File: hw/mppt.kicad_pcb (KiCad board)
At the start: 2 copper layers, 7 parts, among them J1 Conn_01x02, J2 Conn_01x02, Q1 Q_NMOS_DGS, Q2 Q_NMOS_DGS

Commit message: working on documentation, design methmethodology, sizing, layout
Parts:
- removed C1: 10uF, Capacitor_SMD:C_1210_3225Metric
- removed C2: 330uF, Capacitor_THT:CP_Radial_D18.0mm_P7.50mm
- removed J1, J2: Conn_01x02, Connector_PinHeader_2.54mm:PinHeader_1x02_P2.54mm_Horizontal
- removed L1: 1529uH, Inductor_THT:L_CommonMode_Toroid_Vertical_L43.2mm_W22.9mm_Px17.78mm_Py30.48mm_Bourns_8100
- removed Q1, Q2: Q_NMOS_DGS, Package_TO_SOT_SMD:TO-263-2
- added C201: 100nF, Capacitor_SMD:C_0402_1005Metric, B.Cu at (183.2, 77.6)
- added C301: 5uF, Capacitor_THT:CP_Axial_L10.0mm_D6.0mm_P15.00mm_Horizontal, F.Cu at (116.5, 108.8)
- added C302: 18uF, Capacitor_THT:CP_Radial_D10.0mm_P5.00mm, F.Cu at (165.0, 109.6)
- added C303: 18uF, Capacitor_THT:CP_Radial_D10.0mm_P5.00mm, F.Cu at (152.5, 109.5)
- added C304: 18uF, Capacitor_THT:CP_Radial_D10.0mm_P5.00mm, F.Cu at (162.3, 95.5)
- added C401: 100nF, Capacitor_SMD:C_0805_2012Metric, B.Cu at (114.2, 85.4)
- added C402: 100nF, Capacitor_SMD:C_0805_2012Metric, B.Cu at (177.7, 85.6)
- added C403: 100nF, Capacitor_SMD:C_0805_2012Metric, B.Cu at (114.2, 81.4)
- added C404: 100nF, Capacitor_SMD:C_0805_2012Metric, B.Cu at (169.0, 82.6)
- added D202: BLUE, LED_SMD:LED_0805_2012Metric, F.Cu at (107.7, 61.9)
- added D203: YELLOW, LED_SMD:LED_0805_2012Metric, F.Cu at (107.7, 65.0)
- added D204: RED, LED_SMD:LED_0805_2012Metric, F.Cu at (107.7, 68.0)
- added D401: 3.3V Zener, Diode_SMD:D_MiniMELF, B.Cu at (109.5, 82.3)
- added D402: 3.3V Zener, Diode_SMD:D_MiniMELF, B.Cu at (173.6, 82.4)
- added D403: 3.3V Zener, Diode_SMD:D_MiniMELF, B.Cu at (121.7, 81.5)
- added D404: 3.3V Zener, Diode_SMD:D_MiniMELF, B.Cu at (161.5, 81.7)
- added H101: Top Left Mounting Hole, MountingHole:MountingHole_2.2mm_M2, F.Cu at (95.1, 64.9)
- added H102: Top Right Mounting Hole, MountingHole:MountingHole_2.2mm_M2, F.Cu at (187.5, 62.8)
- added H103: Bottom Left Mounting Hole, MountingHole:MountingHole_2.2mm_M2, F.Cu at (94.5, 110.3)
- added H104: Bottom Right Mounting Hole, MountingHole:MountingHole_2.2mm_M2, F.Cu at (188.8, 110.3)
- added J201: 1935776, mppt:1935776, F.Cu at (186.4, 75.1)
- added J301: 1935776, mppt:1935776, F.Cu at (100.2, 103.8)
- added J302: 1935776, mppt:1935776, F.Cu at (183.2, 103.8)
- added Q301: Q_NMOS_DGS, mppt:EPC2307, F.Cu at (152.5, 97.8)
- added Q302: Q_NMOS_DGS, mppt:EPC2307, F.Cu at (156.9, 97.8)
- added R201: 330, Resistor_SMD:R_0805_2012Metric, F.Cu at (112.1, 61.9)
- added R202: 330, Resistor_SMD:R_0805_2012Metric, F.Cu at (112.1, 64.9)
- added R203: 330, Resistor_SMD:R_0805_2012Metric, F.Cu at (112.1, 67.8)
- added R401: 2m, Resistor_SMD:R_1206_3216Metric, F.Cu at (110.0, 98.8)
- added R402: 2m, Resistor_SMD:R_1206_3216Metric, F.Cu at (173.4, 95.5)
- added R403: 100k, Resistor_SMD:R_0805_2012Metric, B.Cu at (118.1, 86.1)
- added R404: 3k, Resistor_SMD:R_0805_2012Metric, B.Cu at (122.4, 86.1)
- added R405: 100k, Resistor_SMD:R_0805_2012Metric, B.Cu at (163.8, 86.3)
- added R406: 2k, Resistor_SMD:R_0805_2012Metric, B.Cu at (168.3, 86.3)
- added SW201: SW_Push, Button_Switch_THT:SW_PUSH_6mm, F.Cu at (173.4, 60.4)
- added TP201: 3.3V TP, TestPoint:TestPoint_Pad_2.0x2.0mm, B.Cu at (125.4, 72.5)
- added TP202: 12V TP, TestPoint:TestPoint_Pad_2.0x2.0mm, B.Cu at (158.3, 72.5)
- added TP203: 5V TP, TestPoint:TestPoint_Pad_2.0x2.0mm, B.Cu at (150.8, 72.5)
- added TP204: GND MCU TP, TestPoint:TestPoint_Pad_2.0x2.0mm, B.Cu at (155.3, 72.5)
- added TP401: GND, TestPoint:TestPoint_Pad_1.0x1.0mm, F.Cu at (108.4, 85.8)
- added TP402: -ARR, TestPoint:TestPoint_Pad_1.0x1.0mm, F.Cu at (111.1, 85.8)
- added TP403: Array Current, TestPoint:TestPoint_Pad_1.0x1.0mm, F.Cu at (107.8, 82.2)
- added TP404: -BATT, TestPoint:TestPoint_Pad_1.0x1.0mm, F.Cu at (174.7, 85.9)
- added TP405: GND, TestPoint:TestPoint_Pad_1.0x1.0mm, F.Cu at (171.9, 85.9)
- added TP406: Battery Current, TestPoint:TestPoint_Pad_1.0x1.0mm, F.Cu at (171.9, 82.4)
- added TP407: +ARR, TestPoint:TestPoint_Pad_1.0x1.0mm, F.Cu at (117.2, 86.1)
- added TP408: Array Voltage, TestPoint:TestPoint_Pad_1.0x1.0mm, F.Cu at (121.7, 79.8)
- added TP409: +BATT, TestPoint:TestPoint_Pad_1.0x1.0mm, F.Cu at (162.9, 86.3)
- added TP410: Battery Voltage, TestPoint:TestPoint_Pad_1.0x1.0mm, F.Cu at (161.5, 80.0)
- added U201: MCU_Nucleo_L432KC, mppt:MODULE_NUCLEO-L432KC, F.Cu at (142.1, 68.1)
- added U401: INA210, Package_TO_SOT_SMD:SOT-363_SC-70-6_Handsoldering, B.Cu at (109.8, 85.8)
- added U402: INA210, Package_TO_SOT_SMD:SOT-363_SC-70-6_Handsoldering, B.Cu at (173.3, 85.9)
- added U403: OPA990, Package_TO_SOT_SMD:SOT-23-6, B.Cu at (117.9, 82.1)
- added U404: OPA990, Package_TO_SOT_SMD:SOT-23-6, B.Cu at (165.3, 82.3)
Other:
- copper layers 2 -> 4
- board text added: "BATT+"
- board text added: "BATT-"
- board text added: "Gate Driver"
- board text added: "Inductor"
- board text added: "Sizing for RM8 Core"
- board text added: "USB ^^^"
- board text added: "VIA FENCE"
- board text removed: "Array Measurement Circuitry"
- board text removed: "Battery Measurement Circuitry"
- board text removed: "Controller"
- board text removed: "Oversized inductor region"

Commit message: parts of gate driver
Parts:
- added C501: 10uF, Capacitor_SMD:C_0402_1005Metric, B.Cu at (155.6, 87.9)
- added C502: 10uF, Capacitor_SMD:C_0402_1005Metric, B.Cu at (153.7, 87.9)
- added R501: 20k, Resistor_SMD:R_0402_1005Metric, B.Cu at (158.1, 90.8)
- added R502: 20k, Resistor_SMD:R_0402_1005Metric, B.Cu at (157.6, 87.9)
- added U501: LMG1210RVRT, mppt:IC_LMG1210RVRT, B.Cu at (154.7, 92.2)
- moved H101 3.51 mm to (92.5, 62.5)
- moved H103 2.94 mm to (92.5, 112.5)
- moved C201 2.55 mm to (181.4, 79.5)
- moved C404 2.55 mm to (167.3, 84.5)
- moved D402 2.55 mm to (171.9, 84.3)
- moved J201 2.55 mm to (184.7, 77.0)
- moved TP404 2.55 mm to (173.0, 87.8)
- moved TP406 2.55 mm to (170.2, 84.3)
- moved U201 2.55 mm to (140.3, 70.0)
- moved SW201 2.55 mm to (171.7, 62.2)
- moved C403 2.55 mm to (112.5, 83.3)
- moved D203 2.55 mm to (106.0, 66.9)
- moved D401 2.55 mm to (107.8, 84.2)
- moved J301 2.55 mm to (98.5, 105.7)
- moved R203 2.55 mm to (110.4, 69.7)
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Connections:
- U201 pad 19: unconnected-(U201-A0-Pad19) -> /controller/PWM_EN
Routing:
- net Net-(U501-DHL): track 0.00 -> 2.72 mm
- net Net-(U501-DLH): track 0.00 -> 2.36 mm
- net +5V: track 0.00 -> 2.19 mm
- net +12V: track 0.00 -> 2.19 mm
- added copper zone on B.Cu, net GND
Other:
- board outline added: 100.1 x 55.1 mm

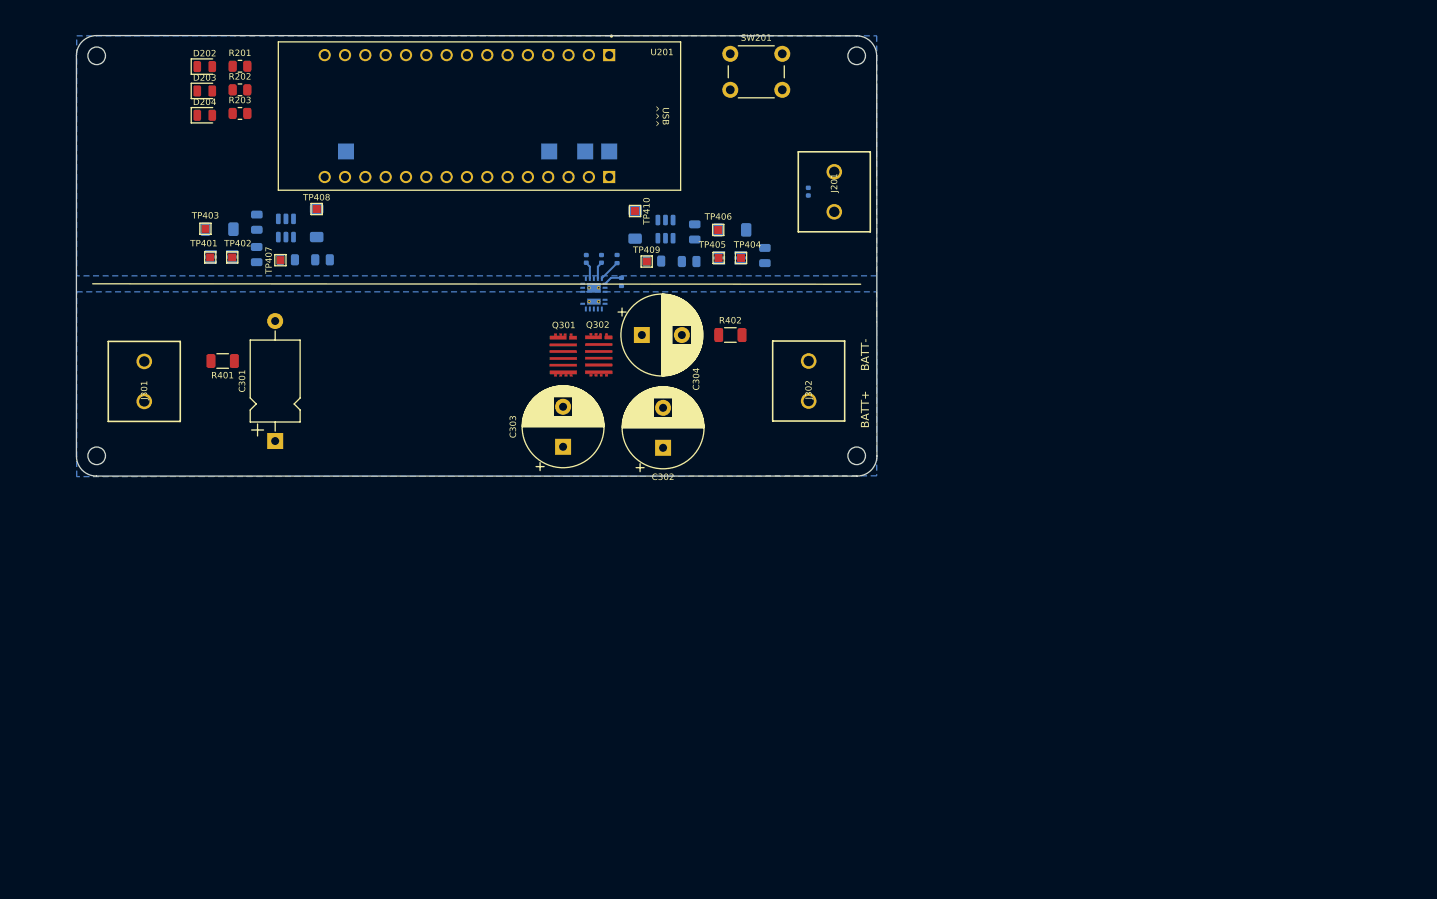
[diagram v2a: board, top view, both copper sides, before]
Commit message: laid out MOSFET switching loop and thermal connections
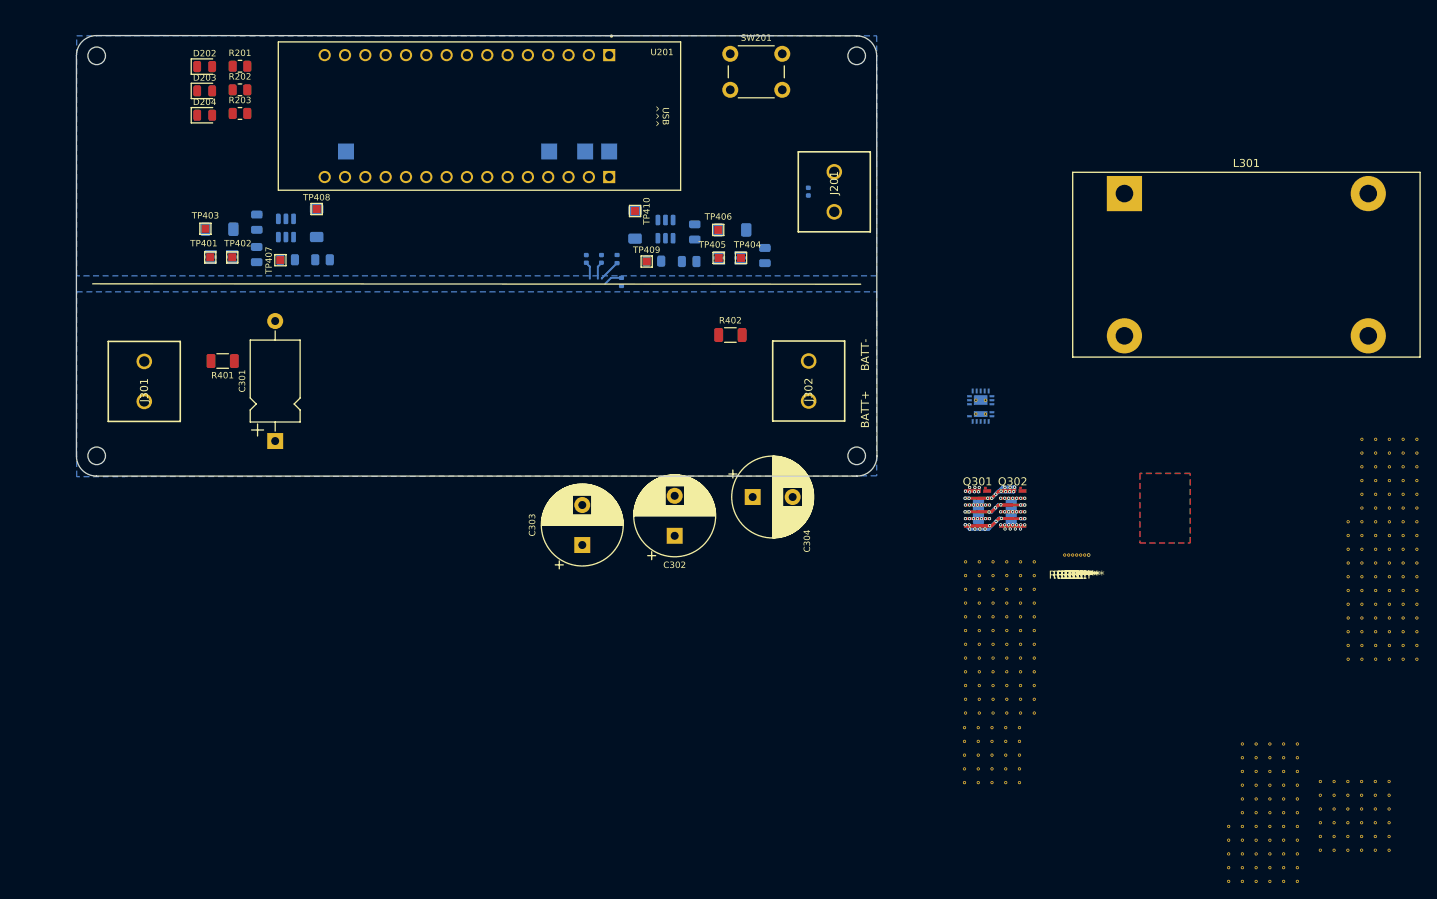
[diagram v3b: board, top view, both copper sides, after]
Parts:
- added C1: 1uF, Capacitor_SMD:C_1812_4532Metric, B.Cu at (204.8, 119.4)
- added L301: 1529uH, Inductor_THT:L_CommonMode_Toroid_Vertical_L43.2mm_W22.9mm_Px17.78mm_Py30.48mm_Bourns_8100, F.Cu at (221.0, 79.7)
- added REF**: Via_0.4mmOD_0.2mmID, mppt:Via_0.4mmOD_0.2mmID, F.Cu at (216.5, 124.9)
- added REF**: Via_0.4mmOD_0.2mmID, mppt:Via_0.4mmOD_0.2mmID, F.Cu at (216.0, 124.9)
- added REF**: Via_0.4mmOD_0.2mmID, mppt:Via_0.4mmOD_0.2mmID, F.Cu at (215.5, 124.9)
- added REF**: Via_0.4mmOD_0.2mmID, mppt:Via_0.4mmOD_0.2mmID, F.Cu at (215.0, 124.9)
- added REF**: Via_0.4mmOD_0.2mmID, mppt:Via_0.4mmOD_0.2mmID, F.Cu at (213.5, 124.9)
- added REF**: Via_0.4mmOD_0.2mmID, mppt:Via_0.4mmOD_0.2mmID, F.Cu at (214.0, 124.9)
- added REF**: Via_0.4mmOD_0.2mmID, mppt:Via_0.4mmOD_0.2mmID, F.Cu at (214.5, 124.9)
- added V1: 0.4mmVia, mppt:Via_0.4mmOD_0.2mmID, F.Cu at (201.1, 125.8)
- added V10: 0.4mmVia, mppt:Via_0.4mmOD_0.2mmID, F.Cu at (201.1, 141.2)
- added V100: 0.4mmVia, mppt:Via_0.4mmOD_0.2mmID, F.Cu at (234.0, 162.3)
- added V101: 0.4mmVia, mppt:Via_0.4mmOD_0.2mmID, F.Cu at (234.0, 164.0)
- added V102: 0.4mmVia, mppt:Via_0.4mmOD_0.2mmID, F.Cu at (234.0, 165.7)
- added V103: 0.4mmVia, mppt:Via_0.4mmOD_0.2mmID, F.Cu at (245.5, 153.2)
- added V104: 0.4mmVia, mppt:Via_0.4mmOD_0.2mmID, F.Cu at (245.5, 154.9)
- added V105: 0.4mmVia, mppt:Via_0.4mmOD_0.2mmID, F.Cu at (245.5, 156.6)
- added V106: 0.4mmVia, mppt:Via_0.4mmOD_0.2mmID, F.Cu at (245.5, 158.4)
- added V107: 0.4mmVia, mppt:Via_0.4mmOD_0.2mmID, F.Cu at (245.5, 160.1)
- added V108: 0.4mmVia, mppt:Via_0.4mmOD_0.2mmID, F.Cu at (245.5, 161.8)
- added V109: 0.4mmVia, mppt:Via_0.4mmOD_0.2mmID, F.Cu at (235.7, 148.5)
- added V11: 0.4mmVia, mppt:Via_0.4mmOD_0.2mmID, F.Cu at (201.1, 142.9)
- added V110: 0.4mmVia, mppt:Via_0.4mmOD_0.2mmID, F.Cu at (235.7, 150.2)
- added V111: 0.4mmVia, mppt:Via_0.4mmOD_0.2mmID, F.Cu at (235.7, 152.0)
- added V112: 0.4mmVia, mppt:Via_0.4mmOD_0.2mmID, F.Cu at (235.7, 153.7)
- added V113: 0.4mmVia, mppt:Via_0.4mmOD_0.2mmID, F.Cu at (235.7, 155.4)
- added V114: 0.4mmVia, mppt:Via_0.4mmOD_0.2mmID, F.Cu at (235.7, 157.1)
- added V115: 0.4mmVia, mppt:Via_0.4mmOD_0.2mmID, F.Cu at (235.7, 158.8)
- added V116: 0.4mmVia, mppt:Via_0.4mmOD_0.2mmID, F.Cu at (235.7, 160.5)
- added V117: 0.4mmVia, mppt:Via_0.4mmOD_0.2mmID, F.Cu at (235.7, 162.3)
- added V118: 0.4mmVia, mppt:Via_0.4mmOD_0.2mmID, F.Cu at (235.7, 164.0)
- added V119: 0.4mmVia, mppt:Via_0.4mmOD_0.2mmID, F.Cu at (235.7, 165.7)
- added V12: 0.4mmVia, mppt:Via_0.4mmOD_0.2mmID, F.Cu at (201.1, 144.7)
- added V120: 0.4mmVia, mppt:Via_0.4mmOD_0.2mmID, F.Cu at (247.2, 153.2)
- added V121: 0.4mmVia, mppt:Via_0.4mmOD_0.2mmID, F.Cu at (247.2, 154.9)
- added V122: 0.4mmVia, mppt:Via_0.4mmOD_0.2mmID, F.Cu at (247.2, 156.6)
- added V123: 0.4mmVia, mppt:Via_0.4mmOD_0.2mmID, F.Cu at (247.2, 158.4)
- added V124: 0.4mmVia, mppt:Via_0.4mmOD_0.2mmID, F.Cu at (247.2, 160.1)
- added V125: 0.4mmVia, mppt:Via_0.4mmOD_0.2mmID, F.Cu at (247.2, 161.8)
- added V126: 0.4mmVia, mppt:Via_0.4mmOD_0.2mmID, F.Cu at (237.4, 148.5)
- added V127: 0.4mmVia, mppt:Via_0.4mmOD_0.2mmID, F.Cu at (237.4, 150.2)
- added V128: 0.4mmVia, mppt:Via_0.4mmOD_0.2mmID, F.Cu at (237.4, 152.0)
- added V129: 0.4mmVia, mppt:Via_0.4mmOD_0.2mmID, F.Cu at (237.4, 153.7)
- added V13: 0.4mmVia, mppt:Via_0.4mmOD_0.2mmID, F.Cu at (201.0, 146.5)
- added V130: 0.4mmVia, mppt:Via_0.4mmOD_0.2mmID, F.Cu at (237.4, 155.4)
- added V131: 0.4mmVia, mppt:Via_0.4mmOD_0.2mmID, F.Cu at (237.4, 157.1)
- added V132: 0.4mmVia, mppt:Via_0.4mmOD_0.2mmID, F.Cu at (237.4, 158.8)
- added V133: 0.4mmVia, mppt:Via_0.4mmOD_0.2mmID, F.Cu at (237.4, 160.5)
- added V134: 0.4mmVia, mppt:Via_0.4mmOD_0.2mmID, F.Cu at (237.4, 162.3)
- added V135: 0.4mmVia, mppt:Via_0.4mmOD_0.2mmID, F.Cu at (237.4, 164.0)
- added V136: 0.4mmVia, mppt:Via_0.4mmOD_0.2mmID, F.Cu at (237.4, 165.7)
- added V137: 0.4mmVia, mppt:Via_0.4mmOD_0.2mmID, F.Cu at (248.9, 153.2)
- added V138: 0.4mmVia, mppt:Via_0.4mmOD_0.2mmID, F.Cu at (248.9, 154.9)
- added V139: 0.4mmVia, mppt:Via_0.4mmOD_0.2mmID, F.Cu at (248.9, 156.6)
- added V14: 0.4mmVia, mppt:Via_0.4mmOD_0.2mmID, F.Cu at (201.0, 148.2)
- added V140: 0.4mmVia, mppt:Via_0.4mmOD_0.2mmID, F.Cu at (248.9, 158.4)
- added V141: 0.4mmVia, mppt:Via_0.4mmOD_0.2mmID, F.Cu at (248.9, 160.1)
- added V142: 0.4mmVia, mppt:Via_0.4mmOD_0.2mmID, F.Cu at (248.9, 161.8)
- added V143: 0.4mmVia, mppt:Via_0.4mmOD_0.2mmID, F.Cu at (239.2, 148.5)
- added V144: 0.4mmVia, mppt:Via_0.4mmOD_0.2mmID, F.Cu at (239.2, 150.2)
- added V145: 0.4mmVia, mppt:Via_0.4mmOD_0.2mmID, F.Cu at (239.2, 152.0)
- added V146: 0.4mmVia, mppt:Via_0.4mmOD_0.2mmID, F.Cu at (239.2, 153.7)
- added V147: 0.4mmVia, mppt:Via_0.4mmOD_0.2mmID, F.Cu at (239.2, 155.4)
- added V148: 0.4mmVia, mppt:Via_0.4mmOD_0.2mmID, F.Cu at (239.2, 157.1)
- added V149: 0.4mmVia, mppt:Via_0.4mmOD_0.2mmID, F.Cu at (239.2, 158.8)
- added V15: 0.4mmVia, mppt:Via_0.4mmOD_0.2mmID, F.Cu at (201.0, 149.9)
- added V150: 0.4mmVia, mppt:Via_0.4mmOD_0.2mmID, F.Cu at (239.2, 160.5)
- added V151: 0.4mmVia, mppt:Via_0.4mmOD_0.2mmID, F.Cu at (239.2, 162.3)
- added V152: 0.4mmVia, mppt:Via_0.4mmOD_0.2mmID, F.Cu at (239.2, 164.0)
- added V153: 0.4mmVia, mppt:Via_0.4mmOD_0.2mmID, F.Cu at (239.2, 165.7)
- added V154: 0.4mmVia, mppt:Via_0.4mmOD_0.2mmID, F.Cu at (250.6, 153.2)
- added V155: 0.4mmVia, mppt:Via_0.4mmOD_0.2mmID, F.Cu at (250.6, 154.9)
- added V156: 0.4mmVia, mppt:Via_0.4mmOD_0.2mmID, F.Cu at (250.6, 156.6)
- added V157: 0.4mmVia, mppt:Via_0.4mmOD_0.2mmID, F.Cu at (250.6, 158.4)
- added V158: 0.4mmVia, mppt:Via_0.4mmOD_0.2mmID, F.Cu at (250.6, 160.1)
- added V159: 0.4mmVia, mppt:Via_0.4mmOD_0.2mmID, F.Cu at (250.6, 161.8)
- added V16: 0.4mmVia, mppt:Via_0.4mmOD_0.2mmID, F.Cu at (201.0, 151.6)
- added V160: 0.4mmVia, mppt:Via_0.4mmOD_0.2mmID, F.Cu at (240.9, 148.5)
- added V161: 0.4mmVia, mppt:Via_0.4mmOD_0.2mmID, F.Cu at (240.9, 150.2)
- added V162: 0.4mmVia, mppt:Via_0.4mmOD_0.2mmID, F.Cu at (240.9, 152.0)
- added V163: 0.4mmVia, mppt:Via_0.4mmOD_0.2mmID, F.Cu at (240.9, 153.7)
- added V164: 0.4mmVia, mppt:Via_0.4mmOD_0.2mmID, F.Cu at (240.9, 155.4)
- added V165: 0.4mmVia, mppt:Via_0.4mmOD_0.2mmID, F.Cu at (240.9, 157.1)
- added V166: 0.4mmVia, mppt:Via_0.4mmOD_0.2mmID, F.Cu at (240.9, 158.8)
- added V167: 0.4mmVia, mppt:Via_0.4mmOD_0.2mmID, F.Cu at (240.9, 160.5)
- added V168: 0.4mmVia, mppt:Via_0.4mmOD_0.2mmID, F.Cu at (240.9, 162.3)
- added V169: 0.4mmVia, mppt:Via_0.4mmOD_0.2mmID, F.Cu at (240.9, 164.0)
- added V17: 0.4mmVia, mppt:Via_0.4mmOD_0.2mmID, F.Cu at (201.0, 153.3)
- added V170: 0.4mmVia, mppt:Via_0.4mmOD_0.2mmID, F.Cu at (240.9, 165.7)
- added V171: 0.4mmVia, mppt:Via_0.4mmOD_0.2mmID, F.Cu at (252.3, 153.2)
- added V172: 0.4mmVia, mppt:Via_0.4mmOD_0.2mmID, F.Cu at (252.3, 154.9)
- added V173: 0.4mmVia, mppt:Via_0.4mmOD_0.2mmID, F.Cu at (252.3, 156.6)
- added V174: 0.4mmVia, mppt:Via_0.4mmOD_0.2mmID, F.Cu at (252.3, 158.4)
- added V175: 0.4mmVia, mppt:Via_0.4mmOD_0.2mmID, F.Cu at (252.3, 160.1)
- added V176: 0.4mmVia, mppt:Via_0.4mmOD_0.2mmID, F.Cu at (252.3, 161.8)
- added V177: 0.4mmVia, mppt:Via_0.4mmOD_0.2mmID, F.Cu at (242.6, 148.5)
- added V178: 0.4mmVia, mppt:Via_0.4mmOD_0.2mmID, F.Cu at (242.6, 150.2)
- added V179: 0.4mmVia, mppt:Via_0.4mmOD_0.2mmID, F.Cu at (242.6, 152.0)
- added V18: 0.4mmVia, mppt:Via_0.4mmOD_0.2mmID, F.Cu at (202.8, 125.8)
- added V180: 0.4mmVia, mppt:Via_0.4mmOD_0.2mmID, F.Cu at (242.6, 153.7)
- added V181: 0.4mmVia, mppt:Via_0.4mmOD_0.2mmID, F.Cu at (242.6, 155.4)
- added V182: 0.4mmVia, mppt:Via_0.4mmOD_0.2mmID, F.Cu at (242.6, 157.1)
- added V183: 0.4mmVia, mppt:Via_0.4mmOD_0.2mmID, F.Cu at (242.6, 158.8)
- added V184: 0.4mmVia, mppt:Via_0.4mmOD_0.2mmID, F.Cu at (242.6, 160.5)
- added V185: 0.4mmVia, mppt:Via_0.4mmOD_0.2mmID, F.Cu at (242.6, 162.3)
- added V186: 0.4mmVia, mppt:Via_0.4mmOD_0.2mmID, F.Cu at (242.6, 164.0)
- added V187: 0.4mmVia, mppt:Via_0.4mmOD_0.2mmID, F.Cu at (242.6, 165.7)
- added V188: 0.4mmVia, mppt:Via_0.4mmOD_0.2mmID, F.Cu at (254.1, 153.2)
- added V189: 0.4mmVia, mppt:Via_0.4mmOD_0.2mmID, F.Cu at (254.1, 154.9)
- added V19: 0.4mmVia, mppt:Via_0.4mmOD_0.2mmID, F.Cu at (202.8, 127.5)
- added V190: 0.4mmVia, mppt:Via_0.4mmOD_0.2mmID, F.Cu at (254.1, 156.6)
- added V191: 0.4mmVia, mppt:Via_0.4mmOD_0.2mmID, F.Cu at (254.1, 158.4)
- added V192: 0.4mmVia, mppt:Via_0.4mmOD_0.2mmID, F.Cu at (254.1, 160.1)
- added V193: 0.4mmVia, mppt:Via_0.4mmOD_0.2mmID, F.Cu at (254.1, 161.8)
- added V194: 0.4mmVia, mppt:Via_0.4mmOD_0.2mmID, F.Cu at (248.9, 120.7)
- added V195: 0.4mmVia, mppt:Via_0.4mmOD_0.2mmID, F.Cu at (248.9, 122.5)
- added V196: 0.4mmVia, mppt:Via_0.4mmOD_0.2mmID, F.Cu at (248.9, 124.2)
- added V197: 0.4mmVia, mppt:Via_0.4mmOD_0.2mmID, F.Cu at (248.9, 125.9)
- added V198: 0.4mmVia, mppt:Via_0.4mmOD_0.2mmID, F.Cu at (248.9, 127.6)
- added V199: 0.4mmVia, mppt:Via_0.4mmOD_0.2mmID, F.Cu at (248.9, 129.3)
- added V2: 0.4mmVia, mppt:Via_0.4mmOD_0.2mmID, F.Cu at (201.1, 127.5)
- added V20: 0.4mmVia, mppt:Via_0.4mmOD_0.2mmID, F.Cu at (202.8, 129.2)
- added V200: 0.4mmVia, mppt:Via_0.4mmOD_0.2mmID, F.Cu at (248.9, 131.1)
- added V201: 0.4mmVia, mppt:Via_0.4mmOD_0.2mmID, F.Cu at (248.9, 132.8)
- added V202: 0.4mmVia, mppt:Via_0.4mmOD_0.2mmID, F.Cu at (248.9, 134.5)
- added V203: 0.4mmVia, mppt:Via_0.4mmOD_0.2mmID, F.Cu at (248.9, 136.2)
- added V204: 0.4mmVia, mppt:Via_0.4mmOD_0.2mmID, F.Cu at (248.9, 137.9)
- added V205: 0.4mmVia, mppt:Via_0.4mmOD_0.2mmID, F.Cu at (250.7, 110.4)
- added V206: 0.4mmVia, mppt:Via_0.4mmOD_0.2mmID, F.Cu at (250.7, 112.2)
- added V207: 0.4mmVia, mppt:Via_0.4mmOD_0.2mmID, F.Cu at (250.7, 113.9)
- added V208: 0.4mmVia, mppt:Via_0.4mmOD_0.2mmID, F.Cu at (250.7, 115.6)
- added V209: 0.4mmVia, mppt:Via_0.4mmOD_0.2mmID, F.Cu at (250.7, 117.3)
- added V21: 0.4mmVia, mppt:Via_0.4mmOD_0.2mmID, F.Cu at (202.8, 130.9)
- added V210: 0.4mmVia, mppt:Via_0.4mmOD_0.2mmID, F.Cu at (250.7, 119.0)
- added V211: 0.4mmVia, mppt:Via_0.4mmOD_0.2mmID, F.Cu at (250.7, 120.7)
- added V212: 0.4mmVia, mppt:Via_0.4mmOD_0.2mmID, F.Cu at (250.7, 122.5)
- added V213: 0.4mmVia, mppt:Via_0.4mmOD_0.2mmID, F.Cu at (250.7, 124.2)
- added V214: 0.4mmVia, mppt:Via_0.4mmOD_0.2mmID, F.Cu at (250.7, 125.9)
- added V215: 0.4mmVia, mppt:Via_0.4mmOD_0.2mmID, F.Cu at (250.7, 127.6)
- added V216: 0.4mmVia, mppt:Via_0.4mmOD_0.2mmID, F.Cu at (250.7, 129.3)
- added V217: 0.4mmVia, mppt:Via_0.4mmOD_0.2mmID, F.Cu at (250.7, 131.1)
- added V218: 0.4mmVia, mppt:Via_0.4mmOD_0.2mmID, F.Cu at (250.7, 132.8)
- added V219: 0.4mmVia, mppt:Via_0.4mmOD_0.2mmID, F.Cu at (250.7, 134.5)
- added V22: 0.4mmVia, mppt:Via_0.4mmOD_0.2mmID, F.Cu at (202.8, 132.6)
- added V220: 0.4mmVia, mppt:Via_0.4mmOD_0.2mmID, F.Cu at (250.7, 136.2)
- added V221: 0.4mmVia, mppt:Via_0.4mmOD_0.2mmID, F.Cu at (250.7, 137.9)
- added V222: 0.4mmVia, mppt:Via_0.4mmOD_0.2mmID, F.Cu at (252.4, 110.4)
- added V223: 0.4mmVia, mppt:Via_0.4mmOD_0.2mmID, F.Cu at (252.4, 112.2)
- added V224: 0.4mmVia, mppt:Via_0.4mmOD_0.2mmID, F.Cu at (252.4, 113.9)
- added V225: 0.4mmVia, mppt:Via_0.4mmOD_0.2mmID, F.Cu at (252.4, 115.6)
- added V226: 0.4mmVia, mppt:Via_0.4mmOD_0.2mmID, F.Cu at (252.4, 117.3)
- added V227: 0.4mmVia, mppt:Via_0.4mmOD_0.2mmID, F.Cu at (252.4, 119.0)
- added V228: 0.4mmVia, mppt:Via_0.4mmOD_0.2mmID, F.Cu at (252.4, 120.7)
- added V229: 0.4mmVia, mppt:Via_0.4mmOD_0.2mmID, F.Cu at (252.4, 122.5)
- added V23: 0.4mmVia, mppt:Via_0.4mmOD_0.2mmID, F.Cu at (202.8, 134.3)
- added V230: 0.4mmVia, mppt:Via_0.4mmOD_0.2mmID, F.Cu at (252.4, 124.2)
- added V231: 0.4mmVia, mppt:Via_0.4mmOD_0.2mmID, F.Cu at (252.4, 125.9)
- added V232: 0.4mmVia, mppt:Via_0.4mmOD_0.2mmID, F.Cu at (252.4, 127.6)
- added V233: 0.4mmVia, mppt:Via_0.4mmOD_0.2mmID, F.Cu at (252.4, 129.3)
- added V234: 0.4mmVia, mppt:Via_0.4mmOD_0.2mmID, F.Cu at (252.4, 131.1)
- added V235: 0.4mmVia, mppt:Via_0.4mmOD_0.2mmID, F.Cu at (252.4, 132.8)
- added V236: 0.4mmVia, mppt:Via_0.4mmOD_0.2mmID, F.Cu at (252.4, 134.5)
- added V237: 0.4mmVia, mppt:Via_0.4mmOD_0.2mmID, F.Cu at (252.4, 136.2)
- added V238: 0.4mmVia, mppt:Via_0.4mmOD_0.2mmID, F.Cu at (252.4, 137.9)
- added V239: 0.4mmVia, mppt:Via_0.4mmOD_0.2mmID, F.Cu at (254.1, 110.4)
- added V24: 0.4mmVia, mppt:Via_0.4mmOD_0.2mmID, F.Cu at (202.8, 136.1)
- added V240: 0.4mmVia, mppt:Via_0.4mmOD_0.2mmID, F.Cu at (254.1, 112.2)
- added V241: 0.4mmVia, mppt:Via_0.4mmOD_0.2mmID, F.Cu at (254.1, 113.9)
- added V242: 0.4mmVia, mppt:Via_0.4mmOD_0.2mmID, F.Cu at (254.1, 115.6)
- added V243: 0.4mmVia, mppt:Via_0.4mmOD_0.2mmID, F.Cu at (254.1, 117.3)
- added V244: 0.4mmVia, mppt:Via_0.4mmOD_0.2mmID, F.Cu at (254.1, 119.0)
- added V245: 0.4mmVia, mppt:Via_0.4mmOD_0.2mmID, F.Cu at (254.1, 120.7)
- added V246: 0.4mmVia, mppt:Via_0.4mmOD_0.2mmID, F.Cu at (254.1, 122.5)
- added V247: 0.4mmVia, mppt:Via_0.4mmOD_0.2mmID, F.Cu at (254.1, 124.2)
- added V248: 0.4mmVia, mppt:Via_0.4mmOD_0.2mmID, F.Cu at (254.1, 125.9)
- added V249: 0.4mmVia, mppt:Via_0.4mmOD_0.2mmID, F.Cu at (254.1, 127.6)
- added V25: 0.4mmVia, mppt:Via_0.4mmOD_0.2mmID, F.Cu at (202.8, 137.8)
- added V250: 0.4mmVia, mppt:Via_0.4mmOD_0.2mmID, F.Cu at (254.1, 129.3)
- added V251: 0.4mmVia, mppt:Via_0.4mmOD_0.2mmID, F.Cu at (254.1, 131.1)
- added V252: 0.4mmVia, mppt:Via_0.4mmOD_0.2mmID, F.Cu at (254.1, 132.8)
- added V253: 0.4mmVia, mppt:Via_0.4mmOD_0.2mmID, F.Cu at (254.1, 134.5)
- added V254: 0.4mmVia, mppt:Via_0.4mmOD_0.2mmID, F.Cu at (254.1, 136.2)
- added V255: 0.4mmVia, mppt:Via_0.4mmOD_0.2mmID, F.Cu at (254.1, 137.9)
- added V256: 0.4mmVia, mppt:Via_0.4mmOD_0.2mmID, F.Cu at (255.8, 110.4)
- added V257: 0.4mmVia, mppt:Via_0.4mmOD_0.2mmID, F.Cu at (255.8, 112.2)
- added V258: 0.4mmVia, mppt:Via_0.4mmOD_0.2mmID, F.Cu at (255.8, 113.9)
- added V259: 0.4mmVia, mppt:Via_0.4mmOD_0.2mmID, F.Cu at (255.8, 115.6)
- added V26: 0.4mmVia, mppt:Via_0.4mmOD_0.2mmID, F.Cu at (202.8, 139.5)
- added V260: 0.4mmVia, mppt:Via_0.4mmOD_0.2mmID, F.Cu at (255.8, 117.3)
- added V261: 0.4mmVia, mppt:Via_0.4mmOD_0.2mmID, F.Cu at (255.8, 119.0)
- added V262: 0.4mmVia, mppt:Via_0.4mmOD_0.2mmID, F.Cu at (255.8, 120.7)
- added V263: 0.4mmVia, mppt:Via_0.4mmOD_0.2mmID, F.Cu at (255.8, 122.5)
- added V264: 0.4mmVia, mppt:Via_0.4mmOD_0.2mmID, F.Cu at (255.8, 124.2)
- added V265: 0.4mmVia, mppt:Via_0.4mmOD_0.2mmID, F.Cu at (255.8, 125.9)
- added V266: 0.4mmVia, mppt:Via_0.4mmOD_0.2mmID, F.Cu at (255.8, 127.6)
- added V267: 0.4mmVia, mppt:Via_0.4mmOD_0.2mmID, F.Cu at (255.8, 129.3)
- added V268: 0.4mmVia, mppt:Via_0.4mmOD_0.2mmID, F.Cu at (255.8, 131.1)
- added V269: 0.4mmVia, mppt:Via_0.4mmOD_0.2mmID, F.Cu at (255.8, 132.8)
- added V27: 0.4mmVia, mppt:Via_0.4mmOD_0.2mmID, F.Cu at (202.8, 141.2)
- added V270: 0.4mmVia, mppt:Via_0.4mmOD_0.2mmID, F.Cu at (255.8, 134.5)
- added V271: 0.4mmVia, mppt:Via_0.4mmOD_0.2mmID, F.Cu at (255.8, 136.2)
- added V272: 0.4mmVia, mppt:Via_0.4mmOD_0.2mmID, F.Cu at (255.8, 137.9)
- added V273: 0.4mmVia, mppt:Via_0.4mmOD_0.2mmID, F.Cu at (257.5, 110.4)
- added V274: 0.4mmVia, mppt:Via_0.4mmOD_0.2mmID, F.Cu at (257.5, 112.2)
- added V275: 0.4mmVia, mppt:Via_0.4mmOD_0.2mmID, F.Cu at (257.5, 113.9)
- added V276: 0.4mmVia, mppt:Via_0.4mmOD_0.2mmID, F.Cu at (257.5, 115.6)
- added V277: 0.4mmVia, mppt:Via_0.4mmOD_0.2mmID, F.Cu at (257.5, 117.3)
- added V278: 0.4mmVia, mppt:Via_0.4mmOD_0.2mmID, F.Cu at (257.5, 119.0)
- added V279: 0.4mmVia, mppt:Via_0.4mmOD_0.2mmID, F.Cu at (257.5, 120.7)
- added V28: 0.4mmVia, mppt:Via_0.4mmOD_0.2mmID, F.Cu at (202.8, 142.9)
- added V280: 0.4mmVia, mppt:Via_0.4mmOD_0.2mmID, F.Cu at (257.5, 122.5)
- added V281: 0.4mmVia, mppt:Via_0.4mmOD_0.2mmID, F.Cu at (257.5, 124.2)
- added V282: 0.4mmVia, mppt:Via_0.4mmOD_0.2mmID, F.Cu at (257.5, 125.9)
- added V283: 0.4mmVia, mppt:Via_0.4mmOD_0.2mmID, F.Cu at (257.5, 127.6)
- added V284: 0.4mmVia, mppt:Via_0.4mmOD_0.2mmID, F.Cu at (257.5, 129.3)
- added V285: 0.4mmVia, mppt:Via_0.4mmOD_0.2mmID, F.Cu at (257.5, 131.1)
- added V286: 0.4mmVia, mppt:Via_0.4mmOD_0.2mmID, F.Cu at (257.5, 132.8)
- added V287: 0.4mmVia, mppt:Via_0.4mmOD_0.2mmID, F.Cu at (257.5, 134.5)
- added V288: 0.4mmVia, mppt:Via_0.4mmOD_0.2mmID, F.Cu at (257.5, 136.2)
- added V289: 0.4mmVia, mppt:Via_0.4mmOD_0.2mmID, F.Cu at (257.5, 137.9)
- added V29: 0.4mmVia, mppt:Via_0.4mmOD_0.2mmID, F.Cu at (202.8, 144.7)
- added V3: 0.4mmVia, mppt:Via_0.4mmOD_0.2mmID, F.Cu at (201.1, 129.2)
- added V30: 0.4mmVia, mppt:Via_0.4mmOD_0.2mmID, F.Cu at (202.7, 146.5)
- added V31: 0.4mmVia, mppt:Via_0.4mmOD_0.2mmID, F.Cu at (202.7, 148.2)
- added V32: 0.4mmVia, mppt:Via_0.4mmOD_0.2mmID, F.Cu at (202.7, 149.9)
- added V33: 0.4mmVia, mppt:Via_0.4mmOD_0.2mmID, F.Cu at (202.7, 151.6)
- added V34: 0.4mmVia, mppt:Via_0.4mmOD_0.2mmID, F.Cu at (202.7, 153.3)
- added V35: 0.4mmVia, mppt:Via_0.4mmOD_0.2mmID, F.Cu at (204.5, 125.8)
- added V36: 0.4mmVia, mppt:Via_0.4mmOD_0.2mmID, F.Cu at (204.5, 127.5)
- added V37: 0.4mmVia, mppt:Via_0.4mmOD_0.2mmID, F.Cu at (204.5, 129.2)
- added V38: 0.4mmVia, mppt:Via_0.4mmOD_0.2mmID, F.Cu at (204.5, 130.9)
- added V39: 0.4mmVia, mppt:Via_0.4mmOD_0.2mmID, F.Cu at (204.5, 132.6)
- added V4: 0.4mmVia, mppt:Via_0.4mmOD_0.2mmID, F.Cu at (201.1, 130.9)
- added V40: 0.4mmVia, mppt:Via_0.4mmOD_0.2mmID, F.Cu at (204.5, 134.3)
- added V41: 0.4mmVia, mppt:Via_0.4mmOD_0.2mmID, F.Cu at (204.5, 136.1)
- added V42: 0.4mmVia, mppt:Via_0.4mmOD_0.2mmID, F.Cu at (204.5, 137.8)
- added V43: 0.4mmVia, mppt:Via_0.4mmOD_0.2mmID, F.Cu at (204.5, 139.5)
- added V44: 0.4mmVia, mppt:Via_0.4mmOD_0.2mmID, F.Cu at (204.5, 141.2)
- added V45: 0.4mmVia, mppt:Via_0.4mmOD_0.2mmID, F.Cu at (204.5, 142.9)
- added V46: 0.4mmVia, mppt:Via_0.4mmOD_0.2mmID, F.Cu at (204.5, 144.7)
- added V47: 0.4mmVia, mppt:Via_0.4mmOD_0.2mmID, F.Cu at (204.4, 146.5)
- added V48: 0.4mmVia, mppt:Via_0.4mmOD_0.2mmID, F.Cu at (204.4, 148.2)
- added V49: 0.4mmVia, mppt:Via_0.4mmOD_0.2mmID, F.Cu at (204.4, 149.9)
- added V5: 0.4mmVia, mppt:Via_0.4mmOD_0.2mmID, F.Cu at (201.1, 132.6)
- added V50: 0.4mmVia, mppt:Via_0.4mmOD_0.2mmID, F.Cu at (204.4, 151.6)
- added V51: 0.4mmVia, mppt:Via_0.4mmOD_0.2mmID, F.Cu at (204.4, 153.3)
- added V52: 0.4mmVia, mppt:Via_0.4mmOD_0.2mmID, F.Cu at (206.3, 125.8)
- added V53: 0.4mmVia, mppt:Via_0.4mmOD_0.2mmID, F.Cu at (206.3, 127.5)
- added V54: 0.4mmVia, mppt:Via_0.4mmOD_0.2mmID, F.Cu at (206.3, 129.2)
- added V55: 0.4mmVia, mppt:Via_0.4mmOD_0.2mmID, F.Cu at (206.3, 130.9)
- added V56: 0.4mmVia, mppt:Via_0.4mmOD_0.2mmID, F.Cu at (206.3, 132.6)
- added V57: 0.4mmVia, mppt:Via_0.4mmOD_0.2mmID, F.Cu at (206.3, 134.3)
- added V58: 0.4mmVia, mppt:Via_0.4mmOD_0.2mmID, F.Cu at (206.3, 136.1)
- added V59: 0.4mmVia, mppt:Via_0.4mmOD_0.2mmID, F.Cu at (206.3, 137.8)
- added V6: 0.4mmVia, mppt:Via_0.4mmOD_0.2mmID, F.Cu at (201.1, 134.3)
- added V60: 0.4mmVia, mppt:Via_0.4mmOD_0.2mmID, F.Cu at (206.3, 139.5)
- added V61: 0.4mmVia, mppt:Via_0.4mmOD_0.2mmID, F.Cu at (206.3, 141.2)
- added V62: 0.4mmVia, mppt:Via_0.4mmOD_0.2mmID, F.Cu at (206.3, 142.9)
- added V63: 0.4mmVia, mppt:Via_0.4mmOD_0.2mmID, F.Cu at (206.3, 144.7)
- added V64: 0.4mmVia, mppt:Via_0.4mmOD_0.2mmID, F.Cu at (206.1, 146.5)
- added V65: 0.4mmVia, mppt:Via_0.4mmOD_0.2mmID, F.Cu at (206.1, 148.2)
- added V66: 0.4mmVia, mppt:Via_0.4mmOD_0.2mmID, F.Cu at (206.1, 149.9)
- added V67: 0.4mmVia, mppt:Via_0.4mmOD_0.2mmID, F.Cu at (206.1, 151.6)
- added V68: 0.4mmVia, mppt:Via_0.4mmOD_0.2mmID, F.Cu at (206.1, 153.3)
- added V69: 0.4mmVia, mppt:Via_0.4mmOD_0.2mmID, F.Cu at (208.0, 125.8)
- added V7: 0.4mmVia, mppt:Via_0.4mmOD_0.2mmID, F.Cu at (201.1, 136.1)
- added V70: 0.4mmVia, mppt:Via_0.4mmOD_0.2mmID, F.Cu at (208.0, 127.5)
- added V71: 0.4mmVia, mppt:Via_0.4mmOD_0.2mmID, F.Cu at (208.0, 129.2)
- added V72: 0.4mmVia, mppt:Via_0.4mmOD_0.2mmID, F.Cu at (208.0, 130.9)
- added V73: 0.4mmVia, mppt:Via_0.4mmOD_0.2mmID, F.Cu at (208.0, 132.6)
- added V74: 0.4mmVia, mppt:Via_0.4mmOD_0.2mmID, F.Cu at (208.0, 134.3)
- added V75: 0.4mmVia, mppt:Via_0.4mmOD_0.2mmID, F.Cu at (208.0, 136.1)
- added V76: 0.4mmVia, mppt:Via_0.4mmOD_0.2mmID, F.Cu at (208.0, 137.8)
- added V77: 0.4mmVia, mppt:Via_0.4mmOD_0.2mmID, F.Cu at (208.0, 139.5)
- added V78: 0.4mmVia, mppt:Via_0.4mmOD_0.2mmID, F.Cu at (208.0, 141.2)
- added V79: 0.4mmVia, mppt:Via_0.4mmOD_0.2mmID, F.Cu at (208.0, 142.9)
- added V8: 0.4mmVia, mppt:Via_0.4mmOD_0.2mmID, F.Cu at (201.1, 137.8)
- added V80: 0.4mmVia, mppt:Via_0.4mmOD_0.2mmID, F.Cu at (208.0, 144.7)
- added V81: 0.4mmVia, mppt:Via_0.4mmOD_0.2mmID, F.Cu at (207.8, 146.5)
- added V82: 0.4mmVia, mppt:Via_0.4mmOD_0.2mmID, F.Cu at (207.8, 148.2)
- added V83: 0.4mmVia, mppt:Via_0.4mmOD_0.2mmID, F.Cu at (207.8, 149.9)
- added V84: 0.4mmVia, mppt:Via_0.4mmOD_0.2mmID, F.Cu at (207.8, 151.6)
- added V85: 0.4mmVia, mppt:Via_0.4mmOD_0.2mmID, F.Cu at (207.8, 153.3)
- added V86: 0.4mmVia, mppt:Via_0.4mmOD_0.2mmID, F.Cu at (209.7, 125.8)
- added V87: 0.4mmVia, mppt:Via_0.4mmOD_0.2mmID, F.Cu at (209.7, 127.5)
- added V88: 0.4mmVia, mppt:Via_0.4mmOD_0.2mmID, F.Cu at (209.7, 129.2)
- added V89: 0.4mmVia, mppt:Via_0.4mmOD_0.2mmID, F.Cu at (209.7, 130.9)
- added V9: 0.4mmVia, mppt:Via_0.4mmOD_0.2mmID, F.Cu at (201.1, 139.5)
- added V90: 0.4mmVia, mppt:Via_0.4mmOD_0.2mmID, F.Cu at (209.7, 132.6)
- added V91: 0.4mmVia, mppt:Via_0.4mmOD_0.2mmID, F.Cu at (209.7, 134.3)
- added V92: 0.4mmVia, mppt:Via_0.4mmOD_0.2mmID, F.Cu at (209.7, 136.1)
- added V93: 0.4mmVia, mppt:Via_0.4mmOD_0.2mmID, F.Cu at (209.7, 137.8)
- added V94: 0.4mmVia, mppt:Via_0.4mmOD_0.2mmID, F.Cu at (209.7, 139.5)
- added V95: 0.4mmVia, mppt:Via_0.4mmOD_0.2mmID, F.Cu at (209.7, 141.2)
- added V96: 0.4mmVia, mppt:Via_0.4mmOD_0.2mmID, F.Cu at (209.7, 142.9)
- added V97: 0.4mmVia, mppt:Via_0.4mmOD_0.2mmID, F.Cu at (209.7, 144.7)
- added V98: 0.4mmVia, mppt:Via_0.4mmOD_0.2mmID, F.Cu at (234.0, 158.8)
- added V99: 0.4mmVia, mppt:Via_0.4mmOD_0.2mmID, F.Cu at (234.0, 160.5)
- Q301: value Q_NMOS_DGS -> SW_L
- Q302: value Q_NMOS_DGS -> SW_H
- moved Q301 55.2 mm to (202.6, 118.9)
- moved Q302 55.2 mm to (207.0, 118.9)
- moved U501 50.4 mm to (203.0, 106.3)
- moved C304 24.5 mm to (174.5, 117.7)
- moved C303 12.5 mm to (153.2, 123.7)
- moved C302 11.1 mm to (164.8, 122.5)
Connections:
- net Net-(Q301-D) renamed /converter/V_SW
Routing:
- net /converter/V_SW: track 0.00 -> 96.6 mm, vias 0 -> 31
- net GND: vias 0 -> 21
- net /converter/V_BATT+: vias 0 -> 25
- added copper zone on B.Cu, net /converter/V_BATT+
- added copper zone on F.Cu, net /converter/V_BATT+
- added copper zone on In1.Cu, net /converter/V_BATT+
- added copper zone on In2.Cu, net /converter/V_BATT+
